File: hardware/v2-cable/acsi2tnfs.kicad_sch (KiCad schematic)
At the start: 24 parts, among them J1 Debug, J2 To ACSI, J3 To SD card, J4 Debug Header, Q1 BC547, Q2 BC547, U1 SN74LVC245APW, U2 SN74LVC245APW

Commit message: Hardware: v2 and v2-cable, drop v1 and dev
v2 (DB19 on the board) and the new v2-cable (flat cable to a Lotharek DB19
adapter, pass-through header) share one circuit: 74LS07 for /IRQ and /DRQ,
pull-ups on /OE and the 74LS07 inputs, no pull-ups on /IRQ and /DRQ (those
upset the floppy drive when the board is off). v2-cable's box headers are
numbered per row, so pin n is ACSI pin n like on the adapter. Each project
carries its own footprints and fp-lib-table. hardware/README.md explains
both boards. v1, dev and the old gerbers are gone.

Co-Authored-By: Claude Opus 5.5 <noreply@anthropic.com>
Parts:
- removed J1: Debug, Connector_PinHeader_2.54mm:PinHeader_1x03_P2.54mm_Vertical, symbol Connector:Conn_01x03_Socket
- removed J2: To ACSI, Library:PinHeader_2x10_P2.54mm_Vertical_NR_PER_ROW, symbol Connector_Generic:Conn_02x10_Top_Bottom
- removed J4: Debug Header, Library:PinHeader_2x10_P2.54mm_Vertical_NR_PER_ROW, symbol Connector_Generic:Conn_02x10_Top_Bottom
- removed Q1, Q2: BC547, Package_TO_SOT_THT:TO-92_Inline, symbol Transistor_BJT:BC547
- removed R1: 3K3, Resistor_SMD:R_0805_2012Metric, symbol Device:R
- removed R2: 4K7, Resistor_SMD:R_0805_2012Metric, symbol Device:R
- removed R8: 10K, Resistor_SMD:R_0805_2012Metric, symbol Device:R
- added D3, D4: LED, LED_THT:LED_D3.0mm, symbol Device:LED
- added J1: To ACSI, Library:IDC-Header_2x10_P2.54mm_Vertical_NR_PER_ROW, symbol Connector_Generic:Conn_01x20
- added J2: ACSI pass-through, Library:IDC-Header_2x10_P2.54mm_Vertical_NR_PER_ROW, symbol Connector_Generic:Conn_01x20
- added R7: 10K, Resistor_SMD:R_0805_2012Metric, symbol Device:R
- added SW1: SW_Prev, Button_Switch_THT:SW_Tactile_SKHH_Angled, symbol Switch:SW_Push
- added U3: SN74LS07, Package_SO:SOIC-14_3.9x8.7mm_P1.27mm, symbol 74xx:SN74LS07
- C6: value 100pF -> 100n
- R5: value 4K7 -> 10K
- R6: value 3K3 -> 10K
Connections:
- net +3.3V: now also R5.1, R6.1, R7.1; no longer R3.2
- net +5V: now also C6.1, U3.11, U3.13, U3.14 (VCC), U3.5, U3.9; no longer R6.1
- net A1: now also U2.3 (A2), J1.16 (Pin_16), J2.16 (Pin_16); no longer U2.5 (A4)
- net A1_3V3: now also U2.17 (B2); no longer U2.15 (B4)
- net DATA0: now also U1.9 (A8), J1.1 (Pin_1), J2.1 (Pin_1); no longer U1.2 (A1)
- net DATA0_3V3: now also A1.17 (GPIO13), U1.11 (B8); no longer A1.11 (GPIO8), U1.18 (B1)
- net DATA1: now also U1.8 (A7), J1.2 (Pin_2), J2.2 (Pin_2); no longer U1.3 (A2)
- net DATA1_3V3: now also A1.16 (GPIO12), U1.12 (B7); no longer A1.12 (GPIO9), U1.17 (B2)
- net DATA2: now also U1.7 (A6), J1.3 (Pin_3), J2.3 (Pin_3); no longer U1.4 (A3)
- net DATA2_3V3: now also A1.15 (GPIO11), U1.13 (B6); no longer A1.14 (GPIO10), U1.16 (B3)
- net DATA3: now also U1.6 (A5), J1.4 (Pin_4), J2.4 (Pin_4); no longer U1.5 (A4)
- net DATA3_3V3: now also A1.14 (GPIO10), U1.14 (B5); no longer A1.15 (GPIO11), U1.15 (B4)
- net DATA4: now also U1.5 (A4), J1.5 (Pin_5), J2.5 (Pin_5); no longer U1.6 (A5)
- net DATA4_3V3: now also A1.12 (GPIO9), U1.15 (B4); no longer A1.16 (GPIO12), U1.14 (B5)
- net DATA5: now also U1.4 (A3), J1.6 (Pin_6), J2.6 (Pin_6); no longer U1.7 (A6)
- net DATA5_3V3: now also A1.11 (GPIO8), U1.16 (B3); no longer A1.17 (GPIO13), U1.13 (B6)
- net DATA6: now also U1.3 (A2), J1.7 (Pin_7), J2.7 (Pin_7); no longer U1.8 (A7)
- net DATA6_3V3: now also A1.10 (GPIO7), U1.17 (B2); no longer A1.19 (GPIO14), U1.12 (B7)
- net DATA7: now also U1.2 (A1), J1.8 (Pin_8), J2.8 (Pin_8); no longer U1.9 (A8)
- net DATA7_3V3: now also A1.9 (GPIO6), U1.18 (B1); no longer A1.20 (GPIO15), U1.11 (B8)
- net DIR: now also A1.19 (GPIO14); no longer A1.10 (GPIO7)
- net GND: now also C6.2, D3.1 (K), D4.1 (K), J1.11 (Pin_11), J1.13 (Pin_13), J1.15 (Pin_15), J1.17 (Pin_17), J2.11 (Pin_11), J2.13 (Pin_13), J2.15 (Pin_15), J2.17 (Pin_17), SW1.1, U3.7 (GND); no longer U2.11 (B8), U2.12 (B7), U2.13 (B6)
- net R/W: now also U2.2 (A1), J1.18 (Pin_18), J2.18 (Pin_18); no longer U2.6 (A5)
- net R/W_3V3: now also U2.18 (B1); no longer U2.14 (B5)
- net /ACK: now also J1.14 (Pin_14), J2.14 (Pin_14)
- net /CS: now also U2.6 (A5), J1.9 (Pin_9), J2.9 (Pin_9); no longer U2.2 (A1)
- net /CS_3V3: now also U2.14 (B5); no longer U2.18 (B1)
- net /DRQ: now also J1.19 (Pin_19), J2.19 (Pin_19), U3.4; no longer R6.2
- net /IRQ: now also J1.10 (Pin_10), J2.10 (Pin_10), U3.2
- net /OE: now also A1.20 (GPIO15), R5.2; no longer A1.9 (GPIO6)
- net /RESET: now also U2.5 (A4), J1.12 (Pin_12), J2.12 (Pin_12); no longer U2.3 (A2)
- net /RESET_3V3: now also U2.15 (B4); no longer U2.17 (B2)
- net at A1.27 (GPIO21): now also R7.2, U3.1; no longer R5.1
- net at A1.29 (GPIO22): now also R6.2, U3.3; no longer C6.1
- net BUTTON: now reaches A1.31 (GPIO26_ADC0)
- net BUTTON: now also SW1.2
- net at D2.2 (A), R4.1: now also D4.2 (A)
- net at D1.2 (A), R3.1: now also D3.2 (A)
- net UART0_RX: no longer names the net of A1.2 (GPIO1)
- net UART0_TX renamed POWER_LED
- net POWER_LED: now also R3.2
- no-connect marks 6 -> 15
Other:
- note added: "3.3v rail"
- note added: "5v rail"
- note added: "Box headers"
- note added: "Decoupling capacitors"
- note added: "Enable/disable button"
- note added: "Leds"
- note added: "Micro SD card"
- note added: "Optional Micro SD card"
- note added: "Pico W"
- note added: "Pull up"
- note added: "SN74LS07 TTL open collector"
- note added: "U1"
- note added: "U2"
- note added: "U3"
- moved on the sheet: A1, C1, C2, C3, C4, C5, D1, D2, J3, R3, R4, U1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

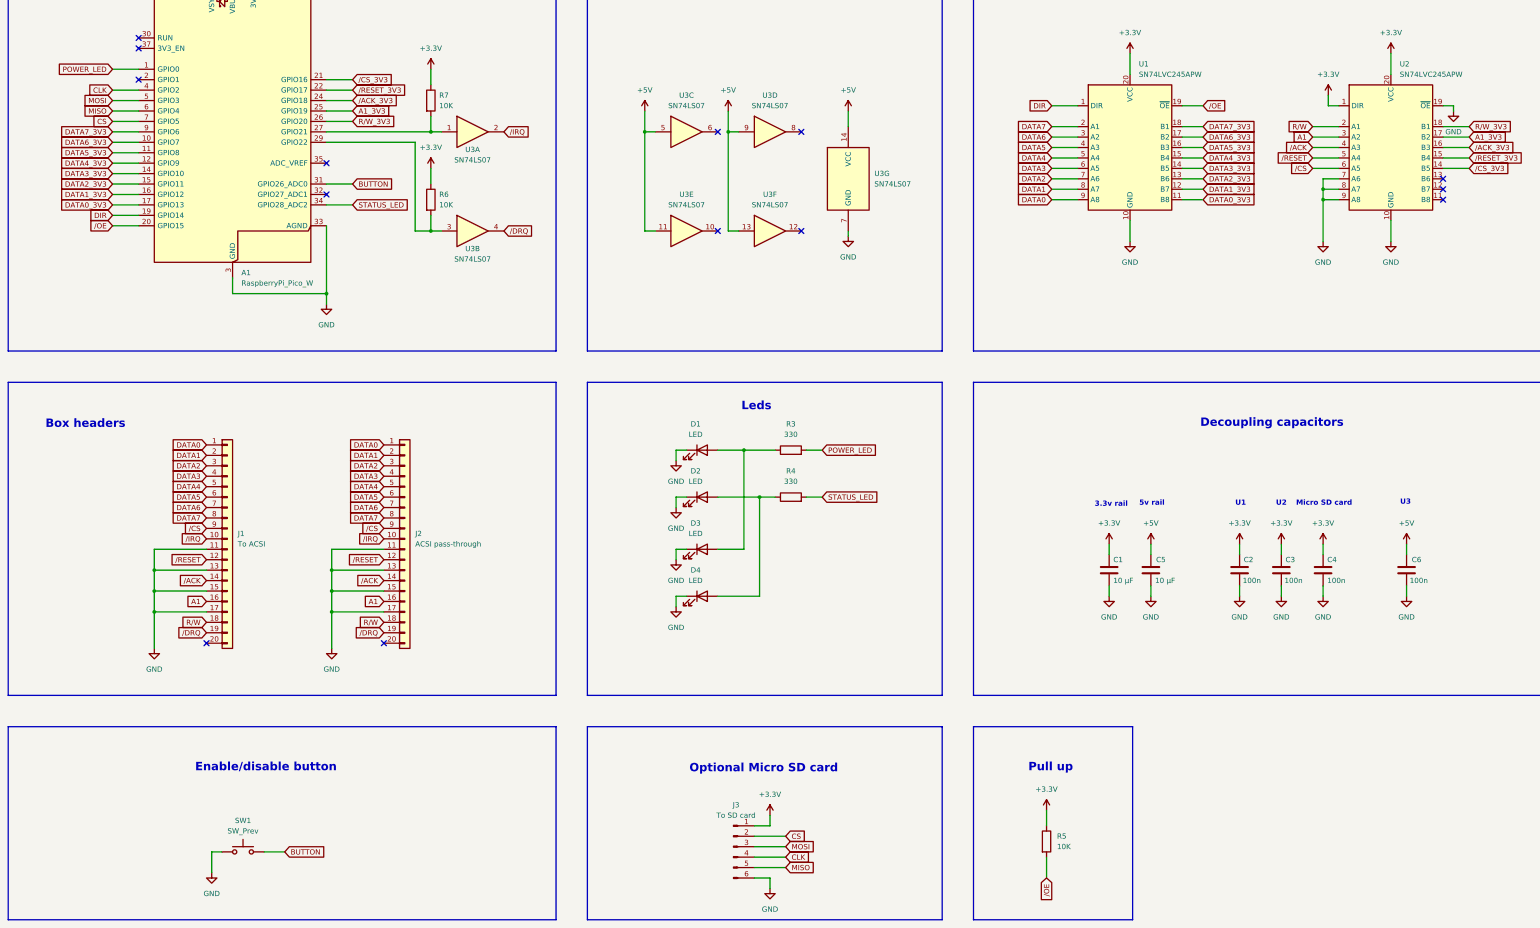
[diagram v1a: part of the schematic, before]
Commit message: hardware/v2-cable: TF-01A micro SD socket on the board, new layout
The SD module is replaced by a TF-01A push-push socket (LCSC C91145) that
sticks out 2.4 mm over the front edge, flush with the case front. Button,
leds and mounting holes moved to fit the 3D-printed case.

Co-Authored-By: Claude Opus 5.5 <noreply@anthropic.com>
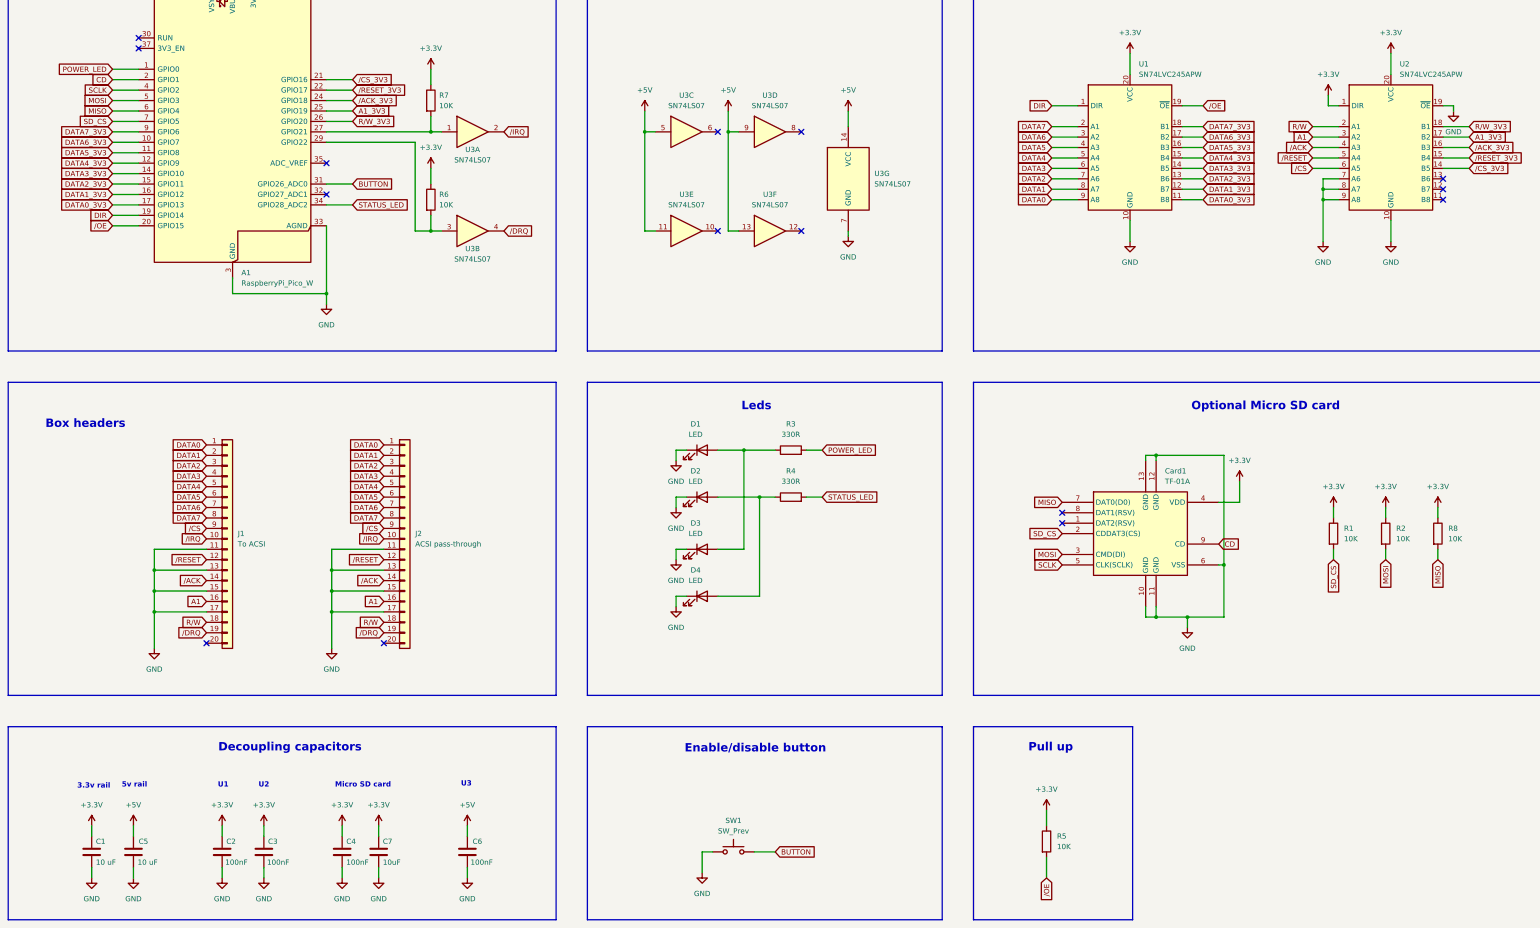
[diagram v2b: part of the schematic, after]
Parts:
- removed J3: To SD card, Connector_PinHeader_2.54mm:PinHeader_1x06_P2.54mm_Vertical, symbol Connector:Conn_01x06_Pin
- added C7: 10uF, Capacitor_SMD:C_0805_2012Metric, symbol Device:C
- added Card1: TF-01A, Micro SD card:TF-SMD_TF-01A, symbol Micro SD card holder:TF-01A
- added R1, R2, R8: 10K, Resistor_SMD:R_0805_2012Metric, symbol Device:R
- C1, C5: value 10 µF -> 10 uF
- C2, C3, C4, C6: value 100n -> 100nF
- R3, R4: value 330 -> 330R
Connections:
- net +3.3V: now also C7.1, Card1.4 (VDD), R1.1, R2.1, R8.1
- net GND: now also C7.2, Card1.10 (GND), Card1.11 (GND), Card1.12 (GND), Card1.13 (GND), Card1.6 (VSS)
- net MISO: now also Card1.7 (DAT0(D0)), R8.2
- net MOSI: now also Card1.3 (CMD(DI)), R2.2
- net CD: now reaches A1.2 (GPIO1)
- net CD: now also Card1.9 (CD)
- net CLK renamed SCLK
- net SCLK: now also Card1.5 (CLK(SCLK))
- net CS renamed SD_CS
- net SD_CS: now also Card1.2 (CDDAT3(CS)), R1.2
- no-connect marks 15 -> 16
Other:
- moved on the sheet: C1, C2, C3, C4, C5, C6, SW1

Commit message: hardware/v2-cable: drop unused library files, update schema.pdf
The TF-01A symbol is stored in the schematic and the 2x10 pin header
footprint is not used. Card1 now uses the footprint from the project
library, so the project no longer needs a global "Micro SD card" library.

Co-Authored-By: Claude Opus 5.5 <noreply@anthropic.com>
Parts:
- Card1: footprint Micro SD card:TF-SMD_TF-01A -> Library:TF-SMD_TF-01A
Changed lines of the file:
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@@
 			)
 		)
-		(property "Footprint" "Micro SD card:TF-SMD_TF-01A"
+		(property "Footprint" "Library:TF-SMD_TF-01A"
 			(at 295.91 208.28 0)
 			(effects

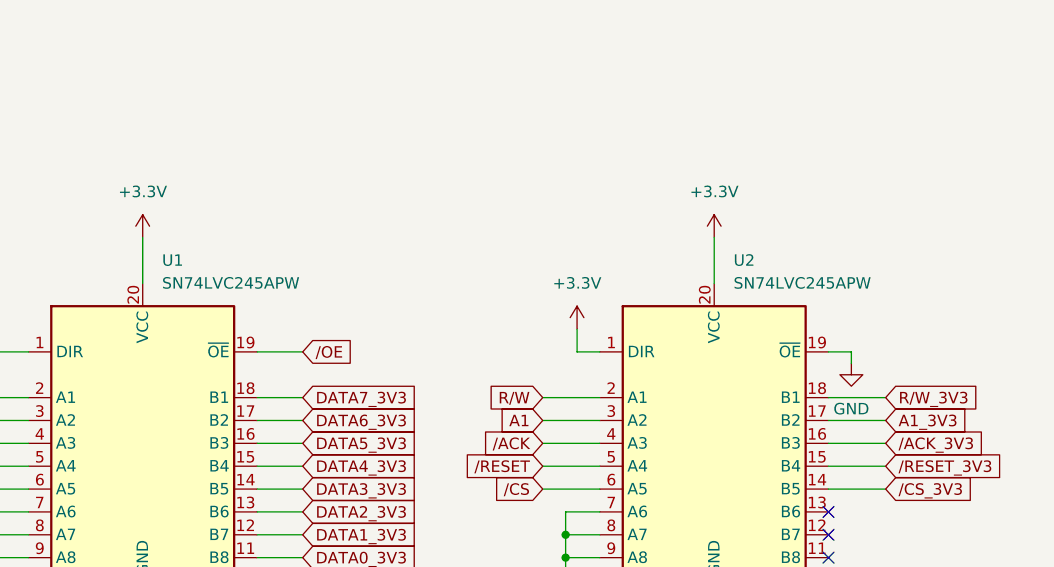
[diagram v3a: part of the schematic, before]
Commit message: hardware: U1/U2 are 74LVC245ADW, silkscreen says ACSI
Both boards: the value of U1/U2 matches the SOIC-20W footprint, the
silkscreen text reads ACSI instead of ASCI, and a stray text outside the
v2 board is gone. schema.pdf and the 3D views updated.

Co-Authored-By: Claude Opus 5.5 <noreply@anthropic.com>
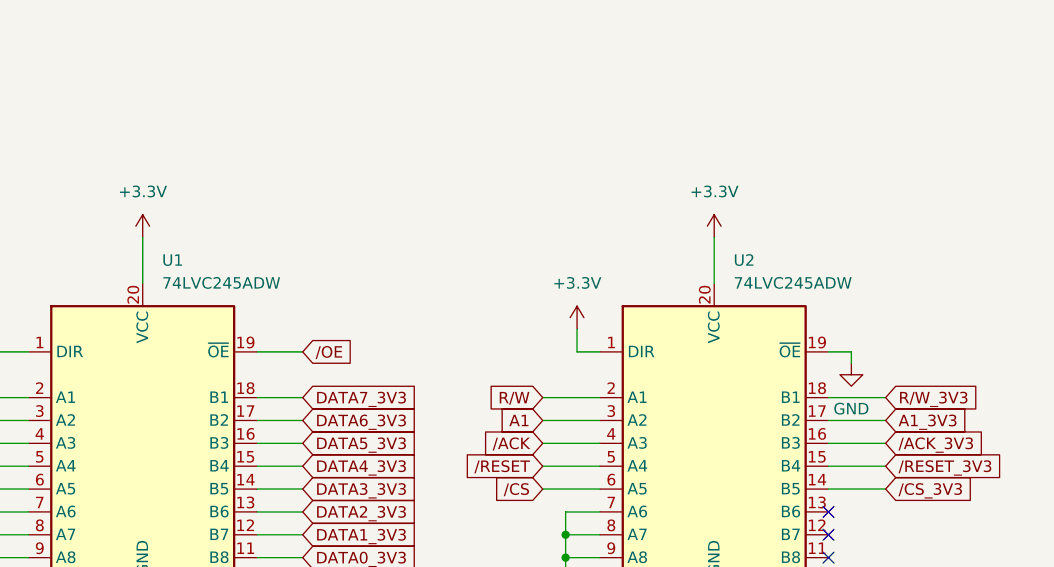
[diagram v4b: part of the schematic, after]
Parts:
- U1, U2: value SN74LVC245APW -> 74LVC245ADW
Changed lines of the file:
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@@
 			)
 		)
-		(property "Value" "SN74LVC245APW"
+		(property "Value" "74LVC245ADW"
 			(at 295.5133 71.12 0)
 			(effects
@@
 			)
 		)
-		(property "Value" "SN74LVC245APW"
+		(property "Value" "74LVC245ADW"
 			(at 359.0133 71.12 0)
 			(effects

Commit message: hardware: D1 yellow, D2 blue, both on 470 ohm
R3 and R4 are 470 ohm in both boards; the led values name the colour
(v2-cable: D3 yellow, D4 blue as well). schema.pdf and the parts list
updated.

Co-Authored-By: Claude Opus 5.5 <noreply@anthropic.com>
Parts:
- D1, D3: value LED -> LED yellow
- D2, D4: value LED -> LED blue
- R3, R4: value 330R -> 470
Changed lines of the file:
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@@
 			)
 		)
-		(property "Value" "LED"
+		(property "Value" "LED blue"
 			(at 187.6425 194.31 0)
 			(effects
@@
 			)
 		)
-		(property "Value" "LED"
+		(property "Value" "LED yellow"
 			(at 187.6425 182.88 0)
 			(effects
@@
 			)
 		)
-		(property "Value" "LED"
+		(property "Value" "LED blue"
 			(at 187.6425 170.18 0)
 			(effects
@@
 			)
 		)
-		(property "Value" "LED"
+		(property "Value" "LED yellow"
 			(at 187.6425 158.75 0)
 			(effects
@@
 			)
 		)
-		(property "Value" "330R"
+		(property "Value" "470"
 			(at 210.82 158.75 90)
 			(effects
@@
 			)
 		)
-		(property "Value" "330R"
+		(property "Value" "470"
 			(at 210.82 170.18 90)
 			(effects
